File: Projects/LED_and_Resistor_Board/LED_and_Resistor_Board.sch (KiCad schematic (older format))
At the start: 0 parts

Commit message: Finish LED_and_Resistor_Board schematic and ERC
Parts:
- added D1: LED, symbol Device:LED
- added R1: R, symbol Device:R
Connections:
- new net: D1.2 (A), R1.2
- new net +5V: R1.1
- new net GND: D1.1 (K)
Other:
- note added: "A simple LED resistor schematic"
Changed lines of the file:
@@
 Comment4 ""
 $EndDescr
+$Comp
+L Device:LED D1
+U 1 1 61C8F6C6
+P 5100 3350
+F 0 "D1" H 5093 3567 50  0000 C CNN
+F 1 "LED" H 5093 3476 50  0000 C CNN
+F 2 "" H 5100 3350 50  0001 C CNN
+F 3 "~" H 5100 3350 50  0001 C CNN
+	1    5100 3350
+	1    0    0    -1
+$EndComp
+$Comp
+L Device:R R1
+U 1 1 61C91682
+P 5650 3350
+F 0 "R1" V 5443 3350 50  0000 C CNN
+F 1 "R" V 5534 3350 50  0000 C CNN
+F 2 "" V 5580 3350 50  0001 C CNN
+F 3 "~" H 5650 3350 50  0001 C CNN
+	1    5650 3350
+	0    1    1    0
+$EndComp
+$Comp
+L power:+5V #PWR02
+U 1 1 61C939FC
+P 6000 2800
+F 0 "#PWR02" H 6000 2650 50  0001 C CNN
+F 1 "+5V" H 6015 2973 50  0000 C CNN
+F 2 "" H 6000 2800 50  0001 C CNN
+F 3 "" H 6000 2800 50  0001 C CNN
+	1    6000 2800
+	1    0    0    -1
+$EndComp
+$Comp
+L power:GND #PWR01
+U 1 1 61C9361C
+P 4650 3550
+F 0 "#PWR01" H 4650 3300 50  0001 C CNN
+F 1 "GND" H 4655 3377 50  0000 C CNN
+F 2 "" H 4650 3550 50  0001 C CNN
+F 3 "" H 4650 3550 50  0001 C CNN
+	1    4650 3550
+	1    0    0    -1
+$EndComp
+Wire Wire Line
+	4950 3350 4650 3350
+Wire Wire Line
+	4650 3350 4650 3550
+Wire Wire Line
+	5250 3350 5500 3350
+Wire Wire Line
+	5800 3350 6000 3350
+Text Label 5850 3350 0    50   ~ 0
+5V
+Text Label 4750 3350 0    50   ~ 0
+GND
+Wire Notes Line
+	4450 2550 6150 2550
+Wire Notes Line
+	6150 2550 6150 3850
+Wire Notes Line
+	6150 3850 4450 3850
+Wire Notes Line
+	4450 3850 4450 2550
+Text Notes 4450 2500 0    50   ~ 0
+A simple LED resistor schematic
+$Comp
+L power:PWR_FLAG #FLG0101
+U 1 1 61C9A493
+P 6300 3000
+F 0 "#FLG0101" H 6300 3075 50  0001 C CNN
+F 1 "PWR_FLAG" V 6300 3128 50  0000 L CNN
+F 2 "" H 6300 3000 50  0001 C CNN
+F 3 "~" H 6300 3000 50  0001 C CNN
+	1    6300 3000
+	0    1    1    0
+$EndComp
+Wire Wire Line
+	6300 3000 6000 3000
+Wire Wire Line
+	6000 3350 6000 3000
+Wire Wire Line
+	6000 3000 6000 2800
+Connection ~ 6000 3000
+$Comp
+L power:PWR_FLAG #FLG0102
+U 1 1 61C9B36F
+P 4200 3350
+F 0 "#FLG0102" H 4200 3425 50  0001 C CNN
+F 1 "PWR_FLAG" V 4200 3477 50  0000 L CNN
+F 2 "" H 4200 3350 50  0001 C CNN
+F 3 "~" H 4200 3350 50  0001 C CNN
+	1    4200 3350
+	0    -1   -1   0
+$EndComp
+Wire Wire Line
+	4200 3350 4650 3350
+Connection ~ 4650 3350
 $EndSCHEMATC

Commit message: Complete symbol and footprint associations for LED and resistor
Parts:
- D1: footprint (none) -> LED_THT:LED_D8.0mm
- R1: footprint (none) -> Resistor_THT:R_Axial_DIN0204_L3.6mm_D1.6mm_P5.08mm_Horizontal
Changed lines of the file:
@@
 F 0 "D1" H 5093 3567 50  0000 C CNN
 F 1 "LED" H 5093 3476 50  0000 C CNN
-F 2 "" H 5100 3350 50  0001 C CNN
+F 2 "LED_THT:LED_D8.0mm" H 5100 3350 50  0001 C CNN
 F 3 "~" H 5100 3350 50  0001 C CNN
 	1    5100 3350
@@
 F 0 "R1" V 5443 3350 50  0000 C CNN
 F 1 "R" V 5534 3350 50  0000 C CNN
-F 2 "" V 5580 3350 50  0001 C CNN
+F 2 "Resistor_THT:R_Axial_DIN0204_L3.6mm_D1.6mm_P5.08mm_Horizontal" V 5580 3350 50  0001 C CNN
 F 3 "~" H 5650 3350 50  0001 C CNN
 	1    5650 3350

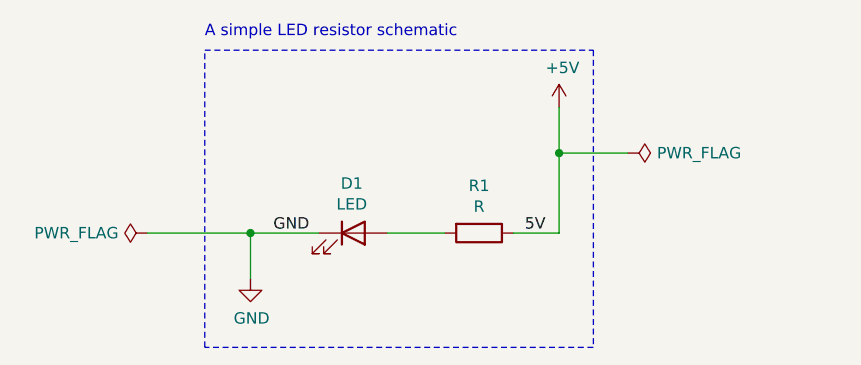
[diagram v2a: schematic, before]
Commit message: Add header to Schematic and change PCB - no more DRC errors
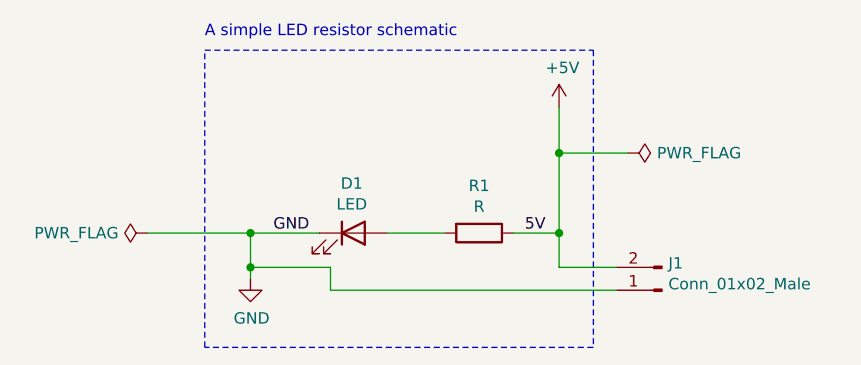
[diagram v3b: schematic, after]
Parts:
- added J1: Conn_01x02_Male, TerminalBlock:TerminalBlock_bornier-2_P5.08mm, symbol Connector:Conn_01x02_Male
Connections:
- net +5V: now also J1.2 (Pin_2)
- net GND: now also J1.1 (Pin_1)
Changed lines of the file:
@@
 	4950 3350 4650 3350
 Wire Wire Line
-	4650 3350 4650 3550
+	4650 3350 4650 3500
 Wire Wire Line
 	5250 3350 5500 3350
@@
 	4200 3350 4650 3350
 Connection ~ 4650 3350
+$Comp
+L Connector:Conn_01x02_Male J1
+U 1 1 61CB92CB
+P 6450 3600
+F 0 "J1" H 6422 3482 50  0000 R CNN
+F 1 "Conn_01x02_Male" H 6422 3573 50  0000 R CNN
+F 2 "TerminalBlock:TerminalBlock_bornier-2_P5.08mm" H 6450 3600 50  0001 C CNN
+F 3 "~" H 6450 3600 50  0001 C CNN
+	1    6450 3600
+	-1   0    0    1
+$EndComp
+Wire Wire Line
+	6250 3500 6000 3500
+Wire Wire Line
+	6000 3500 6000 3350
+Connection ~ 6000 3350
+Wire Wire Line
+	6250 3600 5000 3600
+Wire Wire Line
+	5000 3600 5000 3500
+Wire Wire Line
+	5000 3500 4650 3500
+Connection ~ 4650 3500
+Wire Wire Line
+	4650 3500 4650 3550
 $EndSCHEMATC
